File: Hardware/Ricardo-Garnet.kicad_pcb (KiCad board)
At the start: 4 copper layers, 38.5 x 90 mm, 199 parts, among them IC3 AP2205-W5-7, IC4 TPS61089RNRR, IC5 ADS131M04IRUKR, J1 RBUS, J2 USB_C_Receptacle_USB2.0, J3 3x2 Nanofit, J4 Conn_01x02_Male, J5 Conn_01x02_Male, J7 Conn_01x02_Male, J8 Conn_01x02_Male, J9 Conn_01x02_Male, P4 IN+, P5 IN-, P6 MOTOR1, P7 MOTOR2, P9 MOTOR3, Q1 IRFS7530, Q2 IRFS7530, Q3 IRFS7530, Q4 IRFS7530, Q5 IRFS7530, Q6 IRFS7530, U1 ESP32-S3, U10 MAX31856, U11 MAX31856, U3 DRV8302, U4 LM66200DRLR, U5 SC4215, U6 SN65HVD230, U7 MAX77827AEFD+T, U9 THVD2429, Y2 R940000171

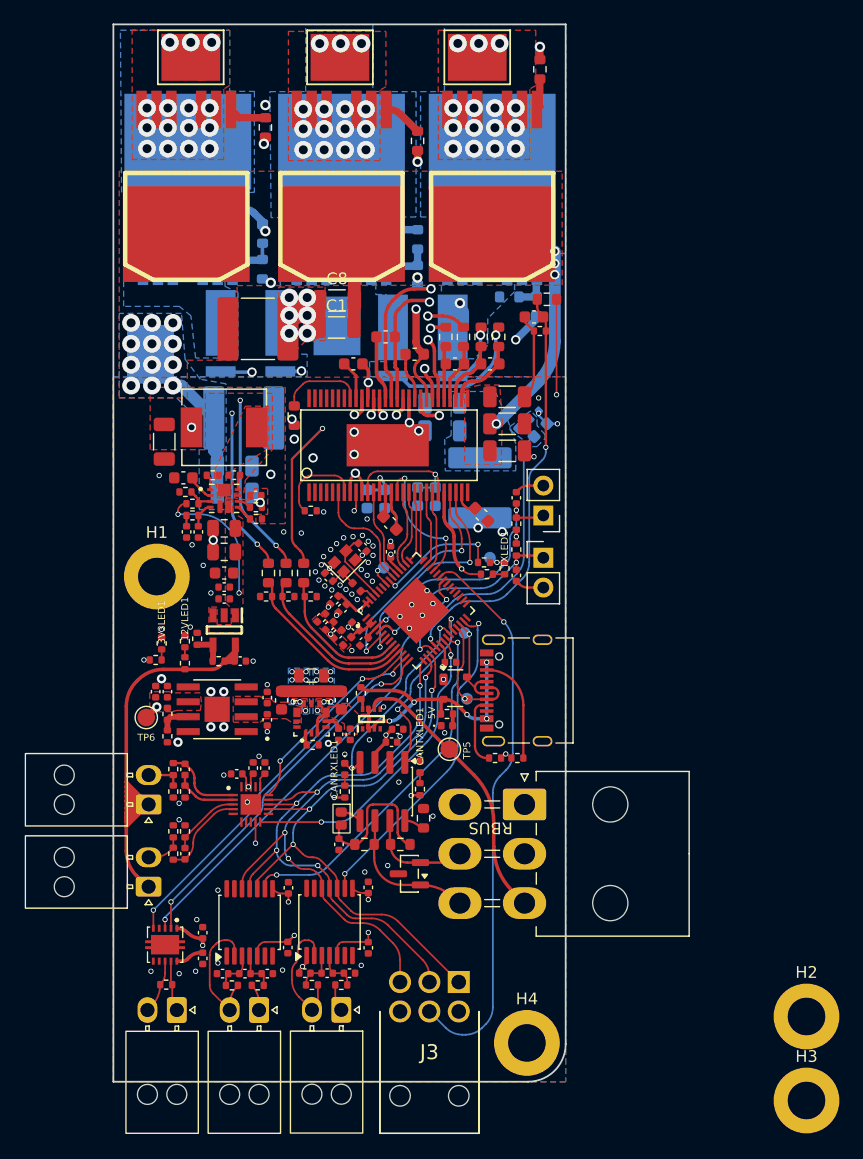
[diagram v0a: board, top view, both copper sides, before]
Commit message: touching up and adding thermals for coating
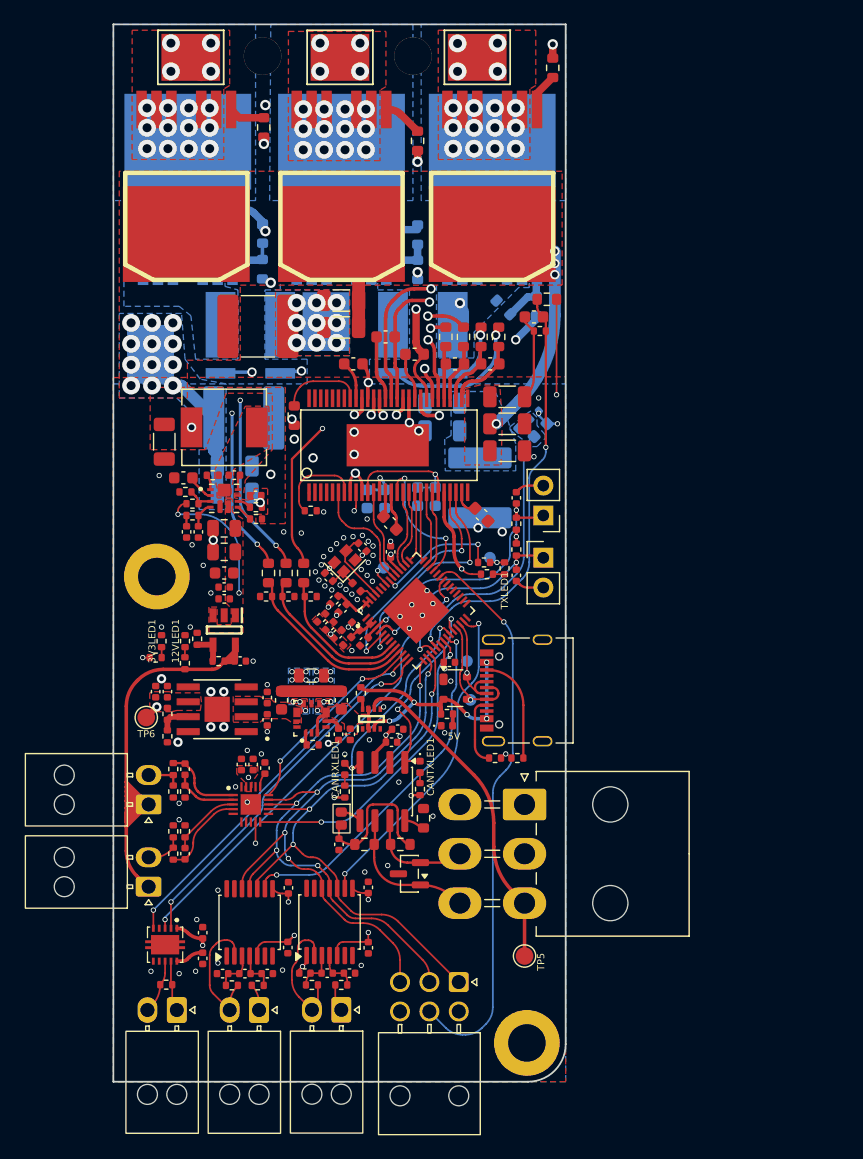
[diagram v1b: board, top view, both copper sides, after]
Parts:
- J3: footprint iclr:1053141206 -> Connector_Molex:Molex_Nano-Fit_105314-xx06_2x03_P2.50mm_Horizontal
- moved H3 100.2 mm to (91.2, 82.7)
- moved H2 88.3 mm to (104.0, 82.7)
- moved TP5 18.7 mm to (113.5, 159.3)
- moved TP2 2.41 mm to (108.6, 134.2)
- moved R28 1.10 mm to (115.9, 83.7)
- moved R30 1.03 mm to (111.7, 104.1), turned to -45 degrees
- moved GND 1.00 mm to (96.6, 105.3)
- moved C77 0.89 mm to (89.4, 143.0), turned to -90 degrees
- moved R35 0.45 mm to (104.4, 100.9)
- moved C1 0.40 mm to (97.9, 105.8)
- moved R36 0.40 mm to (104.4, 97.9)
- moved C8 0.36 mm to (97.9, 103.5)
- moved TP1 0.32 mm to (108.9, 137.5)
- moved C78 0.30 mm to (90.4, 143.0)
- moved R53 0.23 mm to (104.8, 108.6)
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- renumbered P5 to GND, P4 to POWER
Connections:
- H2 pad 1: GND -> unconnected-(H2-Pad1)
- H3 pad 1: GND -> unconnected-(H3-Pad1)
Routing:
- net GND: track 67.5 -> 41.5 mm, vias 103 -> 107
- net RBUS_uC_V: track 23.9 -> 28.4 mm
- net VCC: track 56.9 -> 54.4 mm
- net Net-(Q2-PadG): track 4.08 -> 5.44 mm
- net +5V: track 22.3 -> 23.4 mm
- net /Data+: track 9.05 -> 9.86 mm
- net V_SUPPLY: track 71.1 -> 70.5 mm
- net /Data-: track 11.0 -> 10.4 mm
- net /Mosfet driver/SH_C: track 97.6 -> 97.0 mm, vias 19 -> 20
- net Net-(Q1-PadG): track 2.71 -> 3.28 mm
- net /Mosfet driver/SH_A: track 84.1 -> 83.5 mm, vias 17 -> 18
- net /Mosfet driver/GL_A: track 25.7 -> 25.2 mm
- net /Mosfet driver/SH_B: track 95.6 -> 95.1 mm, vias 18 -> 19

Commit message: added 2wire sensor and silkscreen
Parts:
- added C501: 10nF, Capacitor_SMD:C_0402_1005Metric, F.Cu at (86.7, 150.1)
- added G***: LOGO, LOGO, B.Cu at (95.1, 141.4)
- added JP501: SolderJumper_2_Open, iclr:small_2_pad_jumper_open, F.Cu at (79.8, 161.3)
- added JP502: SolderJumper_2_Open, iclr:small_2_pad_jumper_open, F.Cu at (80.9, 161.3)
- added R21: 10k, Resistor_SMD:R_0402_1005Metric, F.Cu at (84.1, 153.7)
- added R22: 10k, Resistor_SMD:R_0402_1005Metric, F.Cu at (84.1, 155.1)
- added R501: 59, Resistor_SMD:R_0402_1005Metric, F.Cu at (86.7, 152.9)
- added R502: 1k, Resistor_SMD:R_0402_1005Metric, F.Cu at (87.1, 151.5)
- added R503: 1k, Resistor_SMD:R_0402_1005Metric, F.Cu at (86.1, 151.5)
- 12VLED1, 3V3LED1, TXLED1: footprint Resistor_SMD:R_0402_1005Metric -> LED_SMD:LED_0402_1005Metric
- C80, C83: value 0.1uF -> 100n
- moved TP9 4.91 mm to (113.1, 129.6)
- moved R42 2.13 mm to (91.2, 90.9)
- moved TXLED1 1.62 mm to (111.2, 127.8), turned to -135 degrees
- moved P9 1.29 mm to (110.8, 83.0)
- moved R6 0.75 mm to (110.5, 126.4), turned to 135 degrees
- moved R5 0.58 mm to (109.8, 127.1), turned to -45 degrees
- moved H1 0.40 mm to (81.8, 127.0)
- moved P6 0.39 mm to (84.8, 83.0)
- moved H2 0.39 mm to (104.2, 83.0)
- moved H3 0.30 mm to (91.2, 83.0)
- moved P7 0.20 mm to (97.8, 83.0)
- renumbered POWER to P4, GND to P5
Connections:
- IC5 pad 5: unconnected-(IC5-AIN2P-Pad5) -> /sensors/AIN2P
- IC5 pad 6: unconnected-(IC5-AIN2N-Pad6) -> /sensors/AIN2N
- U1 pad 36: /MOD_DE -> /MOD_DIR
- U9 pad 3: /MOD_DE -> /MOD_DIR
- U9 pad 4: GND -> /MOD_DIR
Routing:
- net /MOD_DIR: track 0.00 -> 41.9 mm, vias 0 -> 2
- net /MOD_DE: track 39.7 -> 0.00 mm, vias 2 -> 0
- net +12V: track 50.9 -> 71.0 mm
- net /sensors/DualConn-: track 0.00 -> 11.0 mm, vias 0 -> 2
- net /Mosfet driver/SH_C: track 97.0 -> 86.1 mm
- net /Mosfet driver/SH_B: track 95.1 -> 86.6 mm
- net Net-(J8-Pin_1): track 4.77 -> 13.1 mm
- net /sensors/AIN2P: track 0.00 -> 4.83 mm
- net /sensors/AIN2N: track 0.00 -> 4.32 mm
- net Net-(J8-Pin_2): track 4.59 -> 6.95 mm
- net VCC: track 54.4 -> 56.7 mm
- net /TXD: track 1.76 -> 3.81 mm
- net /Mosfet driver/GH_C: track 37.3 -> 35.6 mm
- net /Mosfet driver/GL_A: track 25.2 -> 23.7 mm
- net /Mosfet driver/SL_A: track 25.5 -> 24.1 mm
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- added copper zone on F.Cu, net /MOD_DIR
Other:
- board text added: "12V"
- board text added: "3V3"
- board text added: "BOOT"
- board text added: "CANRX"
- board text added: "CANTX"
- board text added: "DAT+"
- board text added: "DAT-"
- board text added: "Designed By Jack Crane Electronics 2026"
- board text added: "EN"
- board text added: "GND"
- board text added: "POWER"
- board text added: "RBUS"
- board text added: "RXD"
- board text added: "TXD"

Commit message: changes made post will's review
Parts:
- removed C1, C24, C25, C40, C43, C44, C49, C8, C9: 10u,50V, Capacitor_SMD:C_1206_3216Metric
- removed C18, C20, C23, C26, C41, C52: 2.2u, Capacitor_SMD:C_0603_1608Metric
- removed C19, C21: 2.2n, Capacitor_SMD:C_0603_1608Metric
- removed C2: 100n, Capacitor_SMD:C_0603_1608Metric
- removed C22: 22n, Capacitor_SMD:C_0603_1608Metric
- removed C27, C51: 15u, 100v, Capacitor_SMD:C_2220_5750Metric
- removed C28, C29, C30: 220n, Capacitor_SMD:C_0603_1608Metric
- removed C3: 10uF, Capacitor_SMD:C_0402_1005Metric
- removed C37: 15u,100V, Capacitor_SMD:C_2220_5750Metric
- removed C38: 22uF, Capacitor_SMD:C_0603_1608Metric
- removed C45: 4.7uF, Capacitor_SMD:C_0402_1005Metric
- removed C66: 1uF, Capacitor_SMD:C_0402_1005Metric
- removed C70, C72: 10uF, Capacitor_SMD:C_0805_2012Metric
- removed C71: 2.2uF, Capacitor_SMD:C_0402_1005Metric
- removed C75: 10uF, Capacitor_SMD:C_0603_1608Metric
- removed C76: 100nF, Capacitor_SMD:C_0402_1005Metric
- removed R1: NTC 10k, Resistor_SMD:R_0603_1608Metric
- removed R12, R13, R17, R18: 100R, Resistor_SMD:R_0603_1608Metric
- removed R2, R20: 10k, Resistor_SMD:R_0402_1005Metric
- removed R23, R26, R3, R30, R32, R36, R46: 39k, Resistor_SMD:R_0603_1608Metric
- removed R24, R27, R33, R4: 2k2, Resistor_SMD:R_0402_1005Metric
- removed R25: 1M, Resistor_SMD:R_0603_1608Metric
- removed R28, R29, R34, R35, R42, R43: 4R7, Resistor_SMD:R_0603_1608Metric
- removed R53, R54: SHUNT, CRF1:WSLP2726
- removed TP1, TP2: TestPoint, TestPoint:TestPoint_Pad_D1.0mm
- removed U9: THVD2429, iclr:TPS74901DRCR
- added C114: 100nF, Capacitor_SMD:C_0402_1005Metric, F.Cu at (112.5, 121.6)
- added C115: 2.2uF, Capacitor_SMD:C_0402_1005Metric, F.Cu at (114.8, 104.2)
- added C303: 10uF, Capacitor_SMD:C_0603_1608Metric, F.Cu at (91.3, 137.2)
- added C305: 10uF, Capacitor_SMD:C_0603_1608Metric, F.Cu at (92.8, 137.2)
- added C306: 10uF, Capacitor_SMD:C_0603_1608Metric, F.Cu at (92.8, 140.2)
- added C407: 100nF, Capacitor_SMD:C_0402_1005Metric, F.Cu at (86.4, 124.4)
- added C408: 10uF, Capacitor_SMD:C_0805_2012Metric, F.Cu at (86.6, 125.9)
- added C409: 10uF, Capacitor_SMD:C_0805_2012Metric, F.Cu at (86.6, 127.9)
- added C410: 1uF, Capacitor_SMD:C_0603_1608Metric, F.Cu at (87.8, 134.8)
- added C411: 100nF, Capacitor_SMD:C_0402_1005Metric, F.Cu at (88.2, 133.6)
- added C601: 2.2uF, Capacitor_SMD:C_0402_1005Metric, F.Cu at (101.2, 122.0)
- added C602: 1uF, Capacitor_SMD:C_0402_1005Metric, F.Cu at (106.3, 121.8)
- added C603: 10uF, 50V, Capacitor_SMD:C_1206_3216Metric, B.Cu at (88.0, 111.8)
- added C604: 10uF, 50V, Capacitor_SMD:C_1206_3216Metric, B.Cu at (88.0, 114.2)
- added C605: 15uF, 100V, Capacitor_SMD:C_2220_5750Metric, B.Cu at (89.4, 118.3)
- added C606: 1uF, Capacitor_SMD:C_0402_1005Metric, F.Cu at (108.7, 121.2)
- added C607: 22nF, 50V, Capacitor_SMD:C_0402_1005Metric, F.Cu at (102.5, 121.7)
- added C608: 10uF, 50V, Capacitor_SMD:C_1206_3216Metric, F.Cu at (88.6, 109.3)
- added C609: 10uF, 50V, Capacitor_SMD:C_1206_3216Metric, F.Cu at (88.6, 111.7)
- added C610: 15uF, 100V, Capacitor_SMD:C_2220_5750Metric, F.Cu at (90.2, 105.2)
- added C611: 100nF, 50V, Capacitor_SMD:C_0603_1608Metric, F.Cu at (110.8, 112.3)
- added C612: 10uF, 50V, Capacitor_SMD:C_1206_3216Metric, F.Cu at (111.3, 114.2)
- added C613: 220nF, 50V, Capacitor_SMD:C_0402_1005Metric, F.Cu at (102.1, 109.6)
- added C614: 220nF, 50V, Capacitor_SMD:C_0402_1005Metric, F.Cu at (99.5, 109.6)
- added C615: 220nF, 50V, Capacitor_SMD:C_0402_1005Metric, F.Cu at (104.9, 109.6)
- added C616: 10uF, 50V, Capacitor_SMD:C_1206_3216Metric, F.Cu at (111.3, 119.0)
- added C617: 10uF, 50V, Capacitor_SMD:C_1206_3216Metric, F.Cu at (111.3, 116.6)
- added C618: 15uF, 100V, Capacitor_SMD:C_2220_5750Metric, F.Cu at (113.2, 108.6)
- added C701: 2.2nF, Capacitor_SMD:C_0402_1005Metric, F.Cu at (106.5, 108.1)
- added C702: 2.2nF, Capacitor_SMD:C_0402_1005Metric, F.Cu at (108.5, 109.6)
- added R109: 39kΩ, Resistor_SMD:R_0402_1005Metric, F.Cu at (110.6, 120.7)
- added R110: 2.2kΩ, Resistor_SMD:R_0402_1005Metric, F.Cu at (112.5, 120.7)
- added R111: NCU15XH103F6SRC, easyeda2kicad:R0402, F.Cu at (113.8, 103.1)
- added R112: 10kΩ, Resistor_SMD:R_0402_1005Metric, F.Cu at (114.8, 105.2)
- added R601: ~, Resistor_SMD:R_0402_1005Metric, F.Cu at (99.4, 121.2)
- added R602: ~, Resistor_SMD:R_0402_1005Metric, F.Cu at (99.6, 122.1)
- added R603: 10kΩ, Resistor_SMD:R_0402_1005Metric, F.Cu at (97.4, 122.3)
- added R604: 10kΩ, Resistor_SMD:R_0402_1005Metric, F.Cu at (93.4, 118.5)
- added R605: 10kΩ, Resistor_SMD:R_0402_1005Metric, F.Cu at (95.5, 124.8)
- added R606: 1MΩ, Resistor_SMD:R_0402_1005Metric, F.Cu at (94.4, 111.9)
- added R607: 39kΩ, Resistor_SMD:R_0402_1005Metric, F.Cu at (95.3, 131.3)
- added R608: 2.2kΩ, Resistor_SMD:R_0402_1005Metric, F.Cu at (96.2, 132.9)
- added R609: 39kΩ, Resistor_SMD:R_0402_1005Metric, F.Cu at (94.2, 131.5)
- added R610: 2.2kΩ, Resistor_SMD:R_0402_1005Metric, F.Cu at (94.3, 132.9)
- added R611: 39kΩ, Resistor_SMD:R_0402_1005Metric, F.Cu at (93.8, 134.1)
- added R612: 2.2kΩ, Resistor_SMD:R_0402_1005Metric, F.Cu at (99.2, 135.2)
- added R701: 4.7Ω, Resistor_SMD:R_0603_1608Metric, B.Cu at (90.4, 100.8)
- added R702: 4.7Ω, Resistor_SMD:R_0603_1608Metric, F.Cu at (90.7, 87.8)
- added R703: 39kΩ, Resistor_SMD:R_0402_1005Metric, B.Cu at (90.4, 98.3)
- added R704: 100Ω, Resistor_SMD:R_0402_1005Metric, F.Cu at (104.3, 107.7)
- added R705: 100Ω, Resistor_SMD:R_0402_1005Metric, F.Cu at (104.3, 106.7)
- added R706: 10mΩ, easyeda2kicad:RES-SMD_L7.1-W4.6_HOXLR2818, B.Cu at (89.7, 105.5)
- added R707: 4.7Ω, Resistor_SMD:R_0603_1608Metric, B.Cu at (103.4, 100.5)
- added R708: 4.7Ω, Resistor_SMD:R_0603_1608Metric, F.Cu at (103.2, 87.6)
- added R709: 39kΩ, Resistor_SMD:R_0402_1005Metric, B.Cu at (103.5, 97.9)
- added R710: 4.7Ω, Resistor_SMD:R_0603_1608Metric, B.Cu at (115.9, 100.9)
- added R711: 4.7Ω, Resistor_SMD:R_0603_1608Metric, F.Cu at (116.1, 87.4)
- added R712: 39kΩ, Resistor_SMD:R_0402_1005Metric, B.Cu at (115.9, 98.3)
- added R713: 100Ω, Resistor_SMD:R_0402_1005Metric, F.Cu at (108.0, 108.2)
- added R714: 100Ω, Resistor_SMD:R_0402_1005Metric, F.Cu at (109.0, 108.2)
- added R715: 10mΩ, easyeda2kicad:RES-SMD_L7.1-W4.6_HOXLR2818, B.Cu at (105.0, 105.4)
- added U501: THVD2429DRCR, easyeda2kicad:VSON-10_L3.0-W3.0-P0.50-BL-EP_DRC, F.Cu at (82.9, 158.3)
- C101: renamed from C7; footprint Capacitor_SMD:C_0402_1005Metric -> Capacitor_SMD:C_0603_1608Metric
- C104: renamed from C15; value 0.1uF -> 100nF
- C105: renamed from C5; value 0.1uF -> 100nF
- C106: renamed from C4; value 0.1uF -> 100nF
- C109: renamed from C11; value 0.1uF -> 100nF
- C110: renamed from C16; value 0.1uF -> 100nF
- C111: renamed from C13; value 0.1uF -> 100nF
- C202: renamed from C62; footprint Capacitor_SMD:C_0402_1005Metric -> Capacitor_SMD:C_0603_1608Metric
- C304: renamed from C42; footprint Capacitor_SMD:C_0402_1005Metric -> Capacitor_SMD:C_0603_1608Metric
- C308: renamed from C47; value 0.1uF -> 100nF
- C501: renamed from C80; value 100n -> 100nF
- C502: renamed from C92; value 0.01uF -> 10nF
- C503: renamed from C93; value 0.1uF -> 100nF
- C504: renamed from C94; value 0.01uF -> 10nF
- C505: renamed from C95; value 0.01uF -> 10nF
- C506: renamed from C96; value 0.1uF -> 100nF
- C507: renamed from C97; value 0.01uF -> 10nF
- C508: renamed from C99; value 0.1uF -> 100nF
- C509: renamed from C98; value 0.1uF -> 100nF
- C510: renamed from C83; value 100n -> 100nF
- C511: renamed from C100; value 0.1uF -> 100nF
- C512: renamed from C101; value 0.1uF -> 100nF
- CANRXLED101: renamed from CANRXLED1; value CANRXLED -> ORANGE_LED
- CANTXLED101: renamed from CANTXLED1; value CANTXLED -> GREEN_LED
- D201: renamed from D7; value SM712_SOT23 -> SM712
- L101: renamed from L4; value 2.0nH -> 2nH
- Q701: renamed from Q1; value IRFS7530 -> IRF7749
- R101: renamed from R7; value 10K -> 10kΩ
- R102: renamed from R5; value 470 -> 1kΩ
- R103: renamed from R55; value 1k -> 1kΩ
- R104: renamed from R56; value 1k -> 1kΩ
- R105: renamed from R9; value 470 -> 1kΩ
- R106: renamed from R8; value 10K -> 10kΩ
- R107: renamed from R6; value 499R -> 499Ω
- R108: renamed from R10; value 3k -> 3kΩ
- R201: renamed from R41; value 0 -> 0Ω
- R202: renamed from R44; value 60 -> 60Ω
- R203: renamed from R45; value 60 -> 60Ω
- R301: renamed from R14; value 10k -> 10kΩ
- R302: renamed from R15; value 14k -> 14kΩ
- R303: renamed from R16; value 56k -> 56kΩ
- R304: renamed from R11; value 10k -> 10kΩ
- R401: renamed from R57; value 28.7k -> 28.7kΩ
- R402: renamed from R58; value 866k -> 866kΩ
- R403: renamed from R59; value 92k -> 92kΩ
- R404: renamed from R61; value 10K -> 10kΩ
- R405: renamed from R62; value 332k -> 332kΩ
- R406: renamed from R63; value 280k -> 280kΩ
- R407: renamed from R60; value 49.9k -> 49.9kΩ
- R408: renamed from R65; value 432k -> 432kΩ
- R501: renamed from R21; value 10k -> 10kΩ
- R502: renamed from R22; value 10k -> 10kΩ
- R503: renamed from R73; value 100 -> 100Ω
- R504: renamed from R75; value 100 -> 100Ω
- R505: renamed from R80; value 100 -> 100Ω
- R506: renamed from R81; value 100 -> 100Ω
- R507: renamed from R66; value 120 -> 120Ω
- R508: renamed from R74; value 59 -> 59Ω
- R509: renamed from R501; value 59 -> 59Ω
- R510: renamed from R76; value 1k -> 1kΩ
- R511: renamed from R72; value 1k -> 1kΩ
- R512: renamed from R502; value 1k -> 1kΩ
- R513: renamed from R503; value 1k -> 1kΩ
- R514: renamed from R67; value 59 -> 59Ω
- R515: renamed from R68; value 1k -> 1kΩ
- R516: renamed from R69; value 1k -> 1kΩ
- R801: renamed from R31; value 5.1k -> 5.1kΩ
- R802: renamed from R39; value 5.1k -> 5.1kΩ
- R803: renamed from R40; value 5.1k -> 5.1kΩ
- TP101: renamed from TP9; moved to F.Cu
- moved 3V3LED101 41.7 mm to (111.1, 162.9), turned to 180 degrees
- moved R105 40.0 mm to (111.1, 161.4), turned to 90 degrees
- moved TP302 39.6 mm to (113.5, 162.1)
- moved Q705 26.3 mm to (111.0, 92.1)
- moved P703 26.2 mm to (111.0, 83.1)
- moved Q702 25.8 mm to (84.9, 96.1)
- moved Q706 25.7 mm to (110.5, 95.9)
- moved P701 25.3 mm to (85.5, 83.3)
- moved Q701 25.3 mm to (85.5, 92.2)
- moved R802 10.5 mm to (111.5, 132.0), turned to 180 degrees
- moved LED801 8.42 mm to (114.3, 143.7), turned to 180 degrees
- moved TP101 7.60 mm to (110.2, 122.5), turned to 0 degrees
- moved R803 7.43 mm to (112.4, 143.7)
- moved C406 7.26 mm to (80.1, 122.2)
- moved L401 4.95 mm to (83.5, 116.4)
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- renumbered 12VLED1 to 12VLED101, 3V3LED1 to 3V3LED101, C14 to C102, C6 to C103, C10 to C107, C12 to C108, C31 to C112, C17 to C113, C61 to C201, C63 to C203, C32 to C301, C35 to C302, C46 to C307, C67 to C401, C68 to C402, C69 to C403, C73 to C404, C74 to C405, C48 to C406, C77 to C513, C78 to C514, C79 to C515, C81 to C516, C501 to C517, C82 to C518, D6 to D801, H1 to H101, H2 to H102, H3 to H103, H4 to H104, IC4 to IC401, IC3 to IC402, IC5 to IC501, J1 to J101, J7 to J501, J4 to J502, J8 to J503, J9 to J504, J5 to J505, J3 to J506, J2 to J801, JP1 to JP101, JP5 to JP102, JP4 to JP201, L5 to L102, L3 to L301, L6 to L401, LED6 to LED801, P4 to P101, P5 to P102, P9 to P701, P7 to P702, P6 to P703, Q2 to Q702, Q3 to Q703, Q4 to Q704, Q5 to Q705, Q6 to Q706, TP10 to TP102, TP5 to TP301, TP6 to TP302, TXLED1 to TXLED101, U1 to U101, U6 to U201, U4 to U301, U7 to U302, U5 to U303, U10 to U502, U11 to U503, U3 to U601, Y2 to Y101
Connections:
- net /Mosfet driver/SL_A renamed /Power MOSFETS/GND before shunt1
- net /Mosfet driver/SL_C renamed /Power MOSFETS/GND before shunt2
- net VCC renamed +3V3
- D801 pad 2: +5V -> /Data-
- D801 pad 3: /Data- -> /Data+
- D801 pad 4: /Data+ -> +5V
- U101 pad 10: /SENS1 -> /SENS3
- U101 pad 11: /SENS2 -> /ACD_CLK
- U101 pad 12: /ACD_CLK -> /MOD_DIR
- U101 pad 36: /MOD_DIR -> /ENCODER_CS
- U101 pad 37: /ENCODER_CS -> /BR_SO2
- U101 pad 38: unconnected-(U1-GPIO33-Pad38) -> /BR_SO1
- U101 pad 6: /BR_SO1 -> /SENS1
- U101 pad 7: /BR_SO2 -> /SENS2
- U101 pad 9: /SENS3 -> /OCTW
- U601 pad 11: Net-(U3-DVDD) -> Net-(U601-OC_ADJ)
- U601 pad 23: Net-(U3-DVDD) -> Net-(U601-DVDD)
- U601 pad 28: GND -> AGND
- U601 pad 5: unconnected-(U3-OCTW-Pad5) -> /OCTW
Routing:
- net V_SUPPLY: track 70.5 -> 6.54 mm, vias 16 -> 12
- net +12V: track 71.0 -> 33.9 mm
- net GND: track 40.6 -> 75.0 mm, vias 109 -> 193
- net /Power MOSFETS/GND before shunt1: track 24.1 -> 51.1 mm, vias 2 -> 3
- net /Mosfet driver/SH_C: track 86.1 -> 60.4 mm, vias 20 -> 18
- net /Mosfet driver/SH_B: track 86.6 -> 61.5 mm, vias 19 -> 18
- net Net-(R12-Pad1): track 24.8 -> 0.00 mm, vias 2 -> 0
- net /Mosfet driver/GH_A: track 48.9 -> 28.7 mm
- net Net-(R13-Pad1): track 18.4 -> 0.00 mm, vias 2 -> 0
- net /OCTW: track 0.00 -> 18.2 mm, vias 0 -> 2
- net +3V3: track 56.7 -> 43.7 mm, vias 21 -> 31
- net /BR_SO1: track 20.1 -> 7.29 mm, vias 2 -> 0
- net Net-(R18-Pad1): track 12.7 -> 0.00 mm, vias 1 -> 0
- net /BR_SO2: track 19.3 -> 7.67 mm, vias 2 -> 0
- net Net-(U3-DVDD): track 11.4 -> 0.00 mm, vias 1 -> 0
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- added copper zone on F.Cu, net +12V
- added copper zone on F.Cu, net /AN_IN
- removed copper zone on B.Cu, net /AN_IN
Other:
- board text added: "Garnet v1.0 Designed By Jack Crane Electronics 2026"
- board text removed: "DAT+"
- board text removed: "DAT-"
- board text removed: "Designed By Jack Crane Electronics 2026"

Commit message: fixed mosfet error
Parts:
- Q701: value IRF7749 -> IRFS7530
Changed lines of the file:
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@@
 			)
 		)
-		(property "Value" "IRF7749"
+		(property "Value" "IRFS7530"
 			(at 0 -11.50112 180)
 			(layer "F.SilkS")
@@
 		(name "$teardrop_padvia$")
 		(hatch none 0.1)
-		(priority 30017)
+		(priority 30019)
 		(attr
 			(teardrop
@@
 		(name "$teardrop_padvia$")
 		(hatch none 0.1)
-		(priority 30038)
+		(priority 30024)
 		(attr
 			(teardrop
@@
 		(name "$teardrop_padvia$")
 		(hatch none 0.1)
-		(priority 30039)
+		(priority 30025)
 		(attr
 			(teardrop
@@
 		(name "$teardrop_padvia$")
 		(hatch none 0.1)
-		(priority 30043)
+		(priority 30029)
 		(attr
 			(teardrop
@@
 		(name "$teardrop_padvia$")
 		(hatch none 0.1)
-		(priority 30020)
+		(priority 30021)
 		(attr
 			(teardrop
@@
 		(name "$teardrop_padvia$")
 		(hatch none 0.1)
-		(priority 30042)
+		(priority 30028)
 		(attr
 			(teardrop
@@
 		(name "$teardrop_padvia$")
 		(hatch none 0.1)
-		(priority 30016)
+		(priority 30017)
 		(attr
 			(teardrop
@@
 		(name "$teardrop_padvia$")
 		(hatch none 0.1)
-		(priority 30021)
+		(priority 30023)
 		(attr
 			(teardrop
@@
 		(name "$teardrop_padvia$")
 		(hatch none 0.1)
-		(priority 30041)
+		(priority 30027)
 		(attr
 			(teardrop
@@
 		(name "$teardrop_padvia$")
 		(hatch none 0.1)
-		(priority 30019)
+		(priority 30020)
 		(attr
 			(teardrop
@@
 		(name "$teardrop_padvia$")
 		(hatch none 0.1)
-		(priority 30020)
+		(priority 30016)
 		(attr
 			(teardrop
@@
 		(name "$teardrop_padvia$")
 		(hatch none 0.1)
-		(priority 30040)
+		(priority 30026)
 		(attr
 			(teardrop
